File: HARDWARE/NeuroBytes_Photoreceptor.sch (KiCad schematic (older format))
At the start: 21 parts, among them P1 CONN_01X04, P2 CONN_01X04, P3 CONN_01X07, SW1 SW_PUSH, SW2 SW_PUSH, U1 APDS9007, U2 STM32L011Gx, U3 LD3985M33R

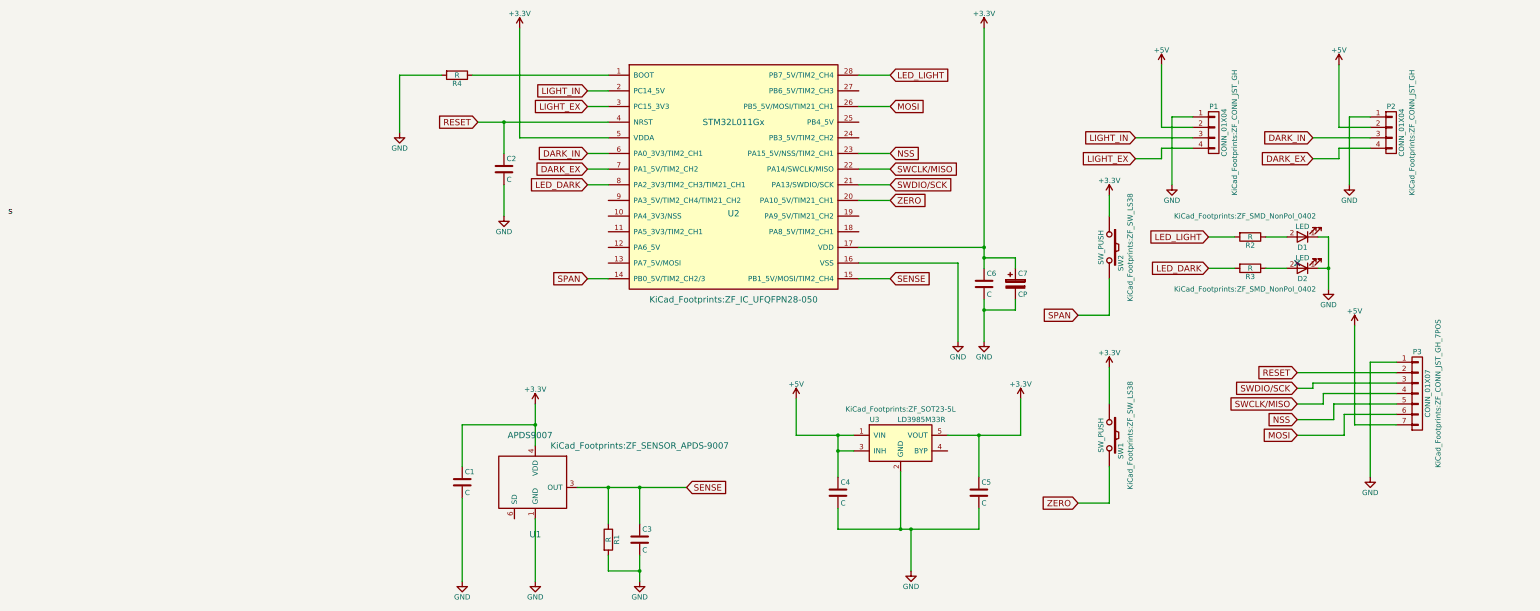
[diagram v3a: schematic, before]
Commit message: Updated Gerber files. Added BOM. Added component values to schematic. Added fiducials.
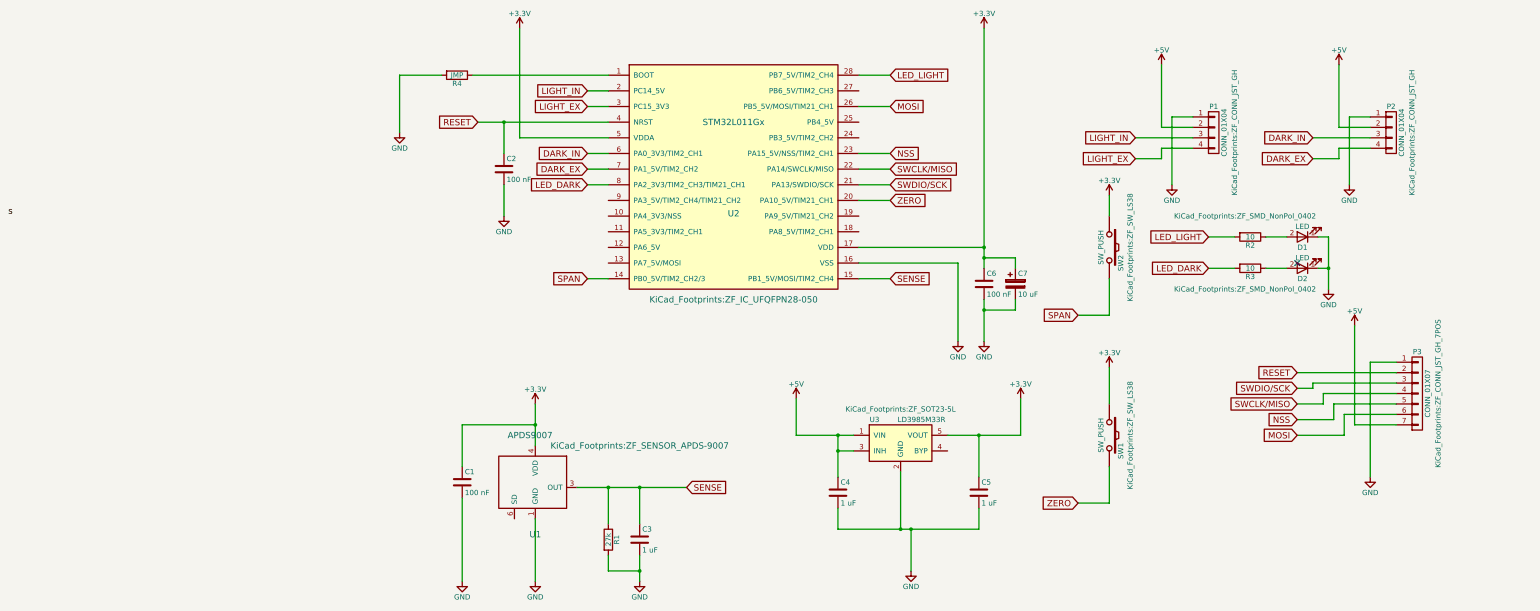
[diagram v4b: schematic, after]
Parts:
- C1, C2, C6: value C -> 100 nF; Subs Allowed No -> Yes
- C3, C4, C5: value C -> 1 uF; Subs Allowed No -> Yes
- C7: value CP -> 10 uF; Subs Allowed No -> Yes
- R1: value R -> 27k; Subs Allowed No -> Yes
- R2, R3: value R -> 10; Subs Allowed No -> Yes
- R4: value R -> JMP; Subs Allowed No -> Yes
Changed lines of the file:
@@
 Sheet 1 1
 Title "Photoreceptor"
-Date "2017-03-04"
-Rev "DRAFT"
+Date "2017-05-16"
+Rev "D"
 Comp "NeuroTinker LLC"
-Comment1 "Ordered 6 boards 3/4/2017 (3 large, 3 small)"
+Comment1 "License: GPL v3"
 Comment2 ""
 Comment3 ""
@@
 $EndComp
 $Comp
-L +5V #PWR8
+L +5V #PWR01
 U 1 1 58B9AB7F
 P 4700 4850
-F 0 "#PWR8" H 4700 4700 50  0001 C CNN
+F 0 "#PWR01" H 4700 4700 50  0001 C CNN
 F 1 "+5V" H 4700 4990 50  0000 C CNN
 F 2 "" H 4700 4850 50  0000 C CNN
@@
 P 5100 5750
 F 0 "C4" H 5125 5850 50  0000 L CNN
-F 1 "C" H 5125 5650 50  0000 L CNN
+F 1 "1 uF" H 5125 5650 50  0000 L CNN
 F 2 "KiCad_Footprints:ZF_SMD_NonPol_0603" H 5138 5600 50  0001 C CNN
 F 3 "" H 5100 5750 50  0000 C CNN
-F 4 "No" H 5100 5750 60  0001 C CNN "Subs Allowed"
+F 4 "Yes" H 5100 5750 60  0001 C CNN "Subs Allowed"
 F 5 "Yes" H 5100 5750 60  0001 C CNN "RoHS"
 	1    5100 5750
@@
 P 6450 5750
 F 0 "C5" H 6475 5850 50  0000 L CNN
-F 1 "C" H 6475 5650 50  0000 L CNN
+F 1 "1 uF" H 6475 5650 50  0000 L CNN
 F 2 "KiCad_Footprints:ZF_SMD_NonPol_0603" H 6488 5600 50  0001 C CNN
 F 3 "" H 6450 5750 50  0000 C CNN
-F 4 "No" H 6450 5750 60  0001 C CNN "Subs Allowed"
+F 4 "Yes" H 6450 5750 60  0001 C CNN "Subs Allowed"
 F 5 "Yes" H 6450 5750 60  0001 C CNN "RoHS"
 	1    6450 5750
@@
 $EndComp
 $Comp
-L +3.3V #PWR13
+L +3.3V #PWR02
 U 1 1 58B9B0DC
 P 6850 4850
-F 0 "#PWR13" H 6850 4700 50  0001 C CNN
+F 0 "#PWR02" H 6850 4700 50  0001 C CNN
 F 1 "+3.3V" H 6850 4990 50  0000 C CNN
 F 2 "" H 6850 4850 50  0000 C CNN
@@
 $EndComp
 $Comp
-L GND #PWR9
+L GND #PWR03
 U 1 1 58B9B110
 P 5800 6500
-F 0 "#PWR9" H 5800 6250 50  0001 C CNN
+F 0 "#PWR03" H 5800 6250 50  0001 C CNN
 F 1 "GND" H 5800 6350 50  0000 C CNN
 F 2 "" H 5800 6500 50  0000 C CNN
@@
 $EndComp
 $Comp
-L +3.3V #PWR4
+L +3.3V #PWR04
 U 1 1 58B9B1C8
 P 2050 1300
-F 0 "#PWR4" H 2050 1150 50  0001 C CNN
+F 0 "#PWR04" H 2050 1150 50  0001 C CNN
 F 1 "+3.3V" H 2050 1440 50  0000 C CNN
 F 2 "" H 2050 1300 50  0000 C CNN
@@
 $EndComp
 $Comp
-L +3.3V #PWR11
+L +3.3V #PWR05
 U 1 1 58B9B218
 P 6500 1300
-F 0 "#PWR11" H 6500 1150 50  0001 C CNN
+F 0 "#PWR05" H 6500 1150 50  0001 C CNN
 F 1 "+3.3V" H 6500 1440 50  0000 C CNN
 F 2 "" H 6500 1300 50  0000 C CNN
@@
 $EndComp
 $Comp
-L GND #PWR10
+L GND #PWR06
 U 1 1 58B9B234
 P 6250 4300
-F 0 "#PWR10" H 6250 4050 50  0001 C CNN
+F 0 "#PWR06" H 6250 4050 50  0001 C CNN
 F 1 "GND" H 6250 4150 50  0000 C CNN
 F 2 "" H 6250 4300 50  0000 C CNN
@@
 P 6500 3750
 F 0 "C6" H 6525 3850 50  0000 L CNN
-F 1 "C" H 6525 3650 50  0000 L CNN
+F 1 "100 nF" H 6525 3650 50  0000 L CNN
 F 2 "KiCad_Footprints:ZF_SMD_NonPol_0402_cap" H 6538 3600 50  0001 C CNN
 F 3 "" H 6500 3750 50  0000 C CNN
-F 4 "No" H 6500 3750 60  0001 C CNN "Subs Allowed"
+F 4 "Yes" H 6500 3750 60  0001 C CNN "Subs Allowed"
 F 5 "Yes" H 6500 3750 60  0001 C CNN "RoHS"
 	1    6500 3750
@@
 $EndComp
 $Comp
-L GND #PWR3
+L GND #PWR07
 U 1 1 58B9B2B4
 P 1900 3100
-F 0 "#PWR3" H 1900 2850 50  0001 C CNN
+F 0 "#PWR07" H 1900 2850 50  0001 C CNN
 F 1 "GND" H 1900 2950 50  0000 C CNN
 F 2 "" H 1900 3100 50  0000 C CNN
@@
 	5600 2800 5300 2800
 $Comp
-L +5V #PWR21
+L +5V #PWR08
 U 1 1 58B9B77D
 P 10050 4150
-F 0 "#PWR21" H 10050 4000 50  0001 C CNN
+F 0 "#PWR08" H 10050 4000 50  0001 C CNN
 F 1 "+5V" H 10050 4290 50  0000 C CNN
 F 2 "" H 10050 4150 50  0000 C CNN
@@
 $EndComp
 $Comp
-L GND #PWR22
+L GND #PWR09
 U 1 1 58B9B796
 P 10200 5600
-F 0 "#PWR22" H 10200 5350 50  0001 C CNN
+F 0 "#PWR09" H 10200 5350 50  0001 C CNN
 F 1 "GND" H 10200 5450 50  0000 C CNN
 F 2 "" H 10200 5600 50  0000 C CNN
@@
 Connection ~ 6500 3400
 $Comp
-L GND #PWR12
+L GND #PWR010
 U 1 1 58B9C6F5
 P 6500 4300
-F 0 "#PWR12" H 6500 4050 50  0001 C CNN
+F 0 "#PWR010" H 6500 4050 50  0001 C CNN
 F 1 "GND" H 6500 4150 50  0000 C CNN
 F 2 "" H 6500 4300 50  0000 C CNN
@@
 P 1900 2650
 F 0 "C2" H 1925 2750 50  0000 L CNN
-F 1 "C" H 1925 2550 50  0000 L CNN
+F 1 "100 nF" H 1925 2550 50  0000 L CNN
 F 2 "KiCad_Footprints:ZF_SMD_NonPol_0402_cap" H 1938 2500 50  0001 C CNN
 F 3 "" H 1900 2650 50  0000 C CNN
-F 4 "No" H 1900 2650 60  0001 C CNN "Subs Allowed"
+F 4 "Yes" H 1900 2650 60  0001 C CNN "Subs Allowed"
 F 5 "Yes" H 1900 2650 60  0001 C CNN "RoHS"
 	1    1900 2650
@@
 $EndComp
 $Comp
-L +5V #PWR19
+L +5V #PWR011
 U 1 1 58B9CBAC
 P 9900 1650
-F 0 "#PWR19" H 9900 1500 50  0001 C CNN
+F 0 "#PWR011" H 9900 1500 50  0001 C CNN
 F 1 "+5V" H 9900 1790 50  0000 C CNN
 F 2 "" H 9900 1650 50  0000 C CNN
@@
 	9900 2250 10200 2250
 $Comp
-L GND #PWR20
+L GND #PWR012
 U 1 1 58B9CC0C
 P 10000 2800
-F 0 "#PWR20" H 10000 2550 50  0001 C CNN
+F 0 "#PWR012" H 10000 2550 50  0001 C CNN
 F 1 "GND" H 10000 2650 50  0000 C CNN
 F 2 "" H 10000 2800 50  0000 C CNN
@@
 $EndComp
 $Comp
-L +5V #PWR16
+L +5V #PWR013
 U 1 1 58B9CEA4
 P 8200 1650
-F 0 "#PWR16" H 8200 1500 50  0001 C CNN
+F 0 "#PWR013" H 8200 1500 50  0001 C CNN
 F 1 "+5V" H 8200 1790 50  0000 C CNN
 F 2 "" H 8200 1650 50  0000 C CNN
@@
 	8200 2250 8500 2250
 $Comp
-L GND #PWR17
+L GND #PWR014
 U 1 1 58B9CEAC
 P 8300 2800
-F 0 "#PWR17" H 8300 2550 50  0001 C CNN
+F 0 "#PWR014" H 8300 2550 50  0001 C CNN
 F 1 "GND" H 8300 2650 50  0000 C CNN
 F 2 "" H 8300 2800 50  0000 C CNN
@@
 $EndComp
 $Comp
-L GND #PWR18
+L GND #PWR015
 U 1 1 58B9D2D7
 P 9800 3800
-F 0 "#PWR18" H 9800 3550 50  0001 C CNN
+F 0 "#PWR015" H 9800 3550 50  0001 C CNN
 F 1 "GND" H 9800 3650 50  0000 C CNN
 F 2 "" H 9800 3800 50  0000 C CNN
@@
 P 9050 3300
 F 0 "R2" V 9130 3300 50  0000 C CNN
-F 1 "R" V 9050 3300 50  0000 C CNN
+F 1 "10" V 9050 3300 50  0000 C CNN
 F 2 "KiCad_Footprints:ZF_SMD_NonPol_0402" V 8980 3300 50  0001 C CNN
 F 3 "" H 9050 3300 50  0000 C CNN
-F 4 "No" H 9050 3300 60  0001 C CNN "Subs Allowed"
+F 4 "Yes" H 9050 3300 60  0001 C CNN "Subs Allowed"
 F 5 "Yes" H 9050 3300 60  0001 C CNN "RoHS"
 	1    9050 3300
@@
 $EndComp
 $Comp
-L +3.3V #PWR15
+L +3.3V #PWR016
 U 1 1 58B9D7AB
 P 7700 4550
-F 0 "#PWR15" H 7700 4400 50  0001 C CNN
+F 0 "#PWR016" H 7700 4400 50  0001 C CNN
 F 1 "+3.3V" H 7700 4690 50  0000 C CNN
 F 2 "" H 7700 4550 50  0000 C CNN
@@
 $EndComp
 $Comp
-L +3.3V #PWR14
+L +3.3V #PWR017
 U 1 1 58B9D91D
 P 7700 2900
-F 0 "#PWR14" H 7700 2750 50  0001 C CNN
+F 0 "#PWR017" H 7700 2750 50  0001 C CNN
 F 1 "+3.3V" H 7700 3040 50  0000 C CNN
 F 2 "" H 7700 2900 50  0000 C CNN
@@
 $EndComp
 $Comp
-L +3.3V #PWR5
+L +3.3V #PWR018
 U 1 1 58B9DDBA
 P 2200 4900
-F 0 "#PWR5" H 2200 4750 50  0001 C CNN
+F 0 "#PWR018" H 2200 4750 50  0001 C CNN
 F 1 "+3.3V" H 2200 5040 50  0000 C CNN
 F 2 "" H 2200 4900 50  0000 C CNN
@@
 	2200 4900 2200 5300
 $Comp
-L GND #PWR6
+L GND #PWR019
 U 1 1 58B9DE4B
 P 2200 6600
-F 0 "#PWR6" H 2200 6350 50  0001 C CNN
+F 0 "#PWR019" H 2200 6350 50  0001 C CNN
 F 1 "GND" H 2200 6450 50  0000 C CNN
 F 2 "" H 2200 6600 50  0000 C CNN
@@
 P 2900 6200
 F 0 "R1" V 2980 6200 50  0000 C CNN
-F 1 "R" V 2900 6200 50  0000 C CNN
+F 1 "27k" V 2900 6200 50  0000 C CNN
 F 2 "KiCad_Footprints:ZF_SMD_NonPol_0402" V 2830 6200 50  0001 C CNN
 F 3 "" H 2900 6200 50  0000 C CNN
-F 4 "No" H 2900 6200 60  0001 C CNN "Subs Allowed"
+F 4 "Yes" H 2900 6200 60  0001 C CNN "Subs Allowed"
 F 5 "Yes" H 2900 6200 60  0001 C CNN "RoHS"
 	1    2900 6200
@@
 P 3200 6200
 F 0 "C3" H 3225 6300 50  0000 L CNN
-F 1 "C" H 3225 6100 50  0000 L CNN
+F 1 "1 uF" H 3225 6100 50  0000 L CNN
 F 2 "KiCad_Footprints:ZF_SMD_NonPol_0603" H 3238 6050 50  0001 C CNN
 F 3 "" H 3200 6200 50  0000 C CNN
-F 4 "No" H 3200 6200 60  0001 C CNN "Subs Allowed"
+F 4 "Yes" H 3200 6200 60  0001 C CNN "Subs Allowed"
 F 5 "Yes" H 3200 6200 60  0001 C CNN "RoHS"
 	1    3200 6200
@@
 $EndComp
 $Comp
-L GND #PWR7
+L GND #PWR020
 U 1 1 58B9DF7E
 P 3200 6600
-F 0 "#PWR7" H 3200 6350 50  0001 C CNN
+F 0 "#PWR020" H 3200 6350 50  0001 C CNN
 F 1 "GND" H 3200 6450 50  0000 C CNN
 F 2 "" H 3200 6600 50  0000 C CNN
@@
 P 1500 5650
 F 0 "C1" H 1525 5750 50  0000 L CNN
-F 1 "C" H 1525 5550 50  0000 L CNN
+F 1 "100 nF" H 1525 5550 50  0000 L CNN
 F 2 "KiCad_Footprints:ZF_SMD_NonPol_0402_cap" H 1538 5500 50  0001 C CNN
 F 3 "" H 1500 5650 50  0000 C CNN
-F 4 "No" H 1500 5650 60  0001 C CNN "Subs Allowed"
+F 4 "Yes" H 1500 5650 60  0001 C CNN "Subs Allowed"
 F 5 "Yes" H 1500 5650 60  0001 C CNN "RoHS"
 	1    1500 5650
@@
 Connection ~ 2200 5100
 $Comp
-L GND #PWR2
+L GND #PWR021
 U 1 1 58B9E313
 P 1500 6600
-F 0 "#PWR2" H 1500 6350 50  0001 C CNN
+F 0 "#PWR021" H 1500 6350 50  0001 C CNN
 F 1 "GND" H 1500 6450 50  0000 C CNN
 F 2 "" H 1500 6600 50  0000 C CNN
@@
 P 9050 3600
 F 0 "R3" V 9130 3600 50  0000 C CNN
-F 1 "R" V 9050 3600 50  0000 C CNN
+F 1 "10" V 9050 3600 50  0000 C CNN
 F 2 "KiCad_Footprints:ZF_SMD_NonPol_0402" V 8980 3600 50  0001 C CNN
 F 3 "" H 9050 3600 50  0000 C CNN
-F 4 "No" H 9050 3600 60  0001 C CNN "Subs Allowed"
+F 4 "Yes" H 9050 3600 60  0001 C CNN "Subs Allowed"
 F 5 "Yes" H 9050 3600 60  0001 C CNN "RoHS"
 	1    9050 3600
@@
 P 1450 1750
 F 0 "R4" V 1530 1750 50  0000 C CNN
-F 1 "R" V 1450 1750 50  0000 C CNN
+F 1 "JMP" V 1450 1750 50  0000 C CNN
 F 2 "KiCad_Footprints:ZF_SMD_NonPol_0402" V 1380 1750 50  0001 C CNN
 F 3 "" H 1450 1750 50  0000 C CNN
-F 4 "No" H 1450 1750 60  0001 C CNN "Subs Allowed"
+F 4 "Yes" H 1450 1750 60  0001 C CNN "Subs Allowed"
 F 5 "Yes" H 1450 1750 60  0001 C CNN "RoHS"
 	1    1450 1750
@@
 $EndComp
 $Comp
-L GND #PWR1
+L GND #PWR022
 U 1 1 590B4A9C
 P 900 2300
-F 0 "#PWR1" H 900 2050 50  0001 C CNN
+F 0 "#PWR022" H 900 2050 50  0001 C CNN
 F 1 "GND" H 900 2150 50  0000 C CNN
 F 2 "" H 900 2300 50  0000 C CNN
@@
 P 6800 3750
 F 0 "C7" H 6825 3850 50  0000 L CNN
-F 1 "CP" H 6825 3650 50  0000 L CNN
+F 1 "10 uF" H 6825 3650 50  0000 L CNN
 F 2 "KiCad_Footprints:ZF_SMD_pol_1206" H 6838 3600 50  0001 C CNN
 F 3 "" H 6800 3750 50  0000 C CNN
-F 4 "No" H 6800 3750 60  0001 C CNN "Subs Allowed"
+F 4 "Yes" H 6800 3750 60  0001 C CNN "Subs Allowed"
 F 5 "Yes" H 6800 3750 60  0001 C CNN "RoHS"
 	1    6800 3750

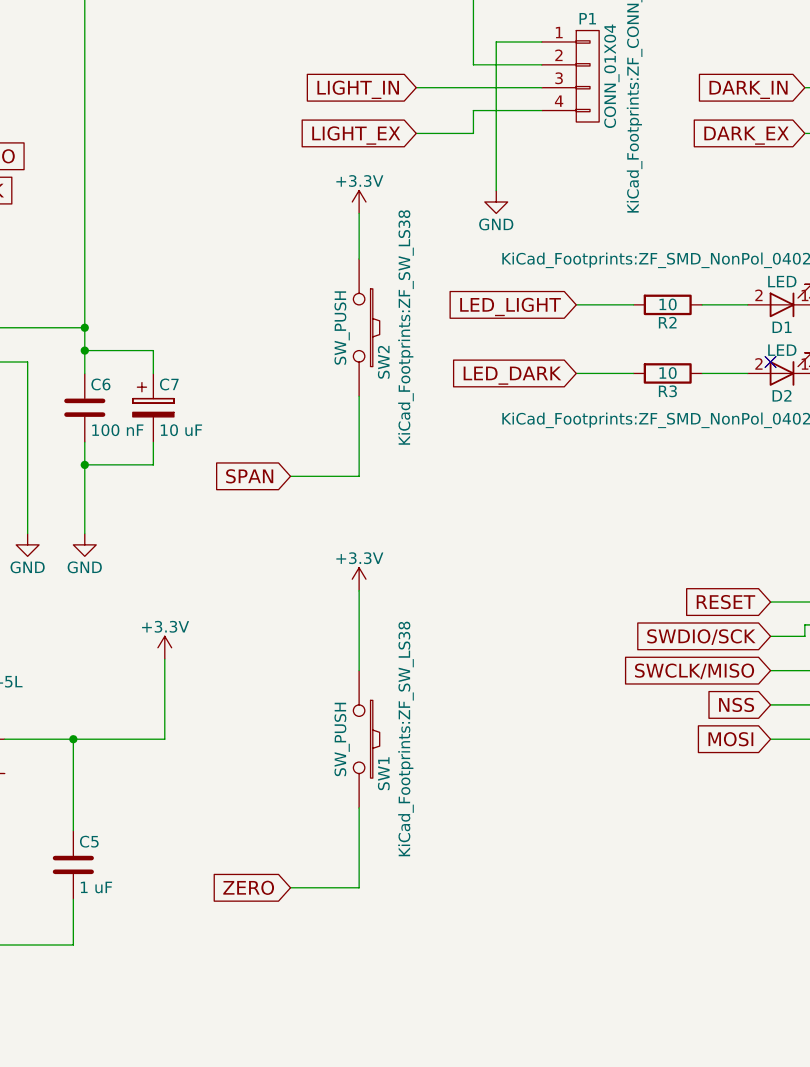
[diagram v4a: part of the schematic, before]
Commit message: Updated swith footprint.
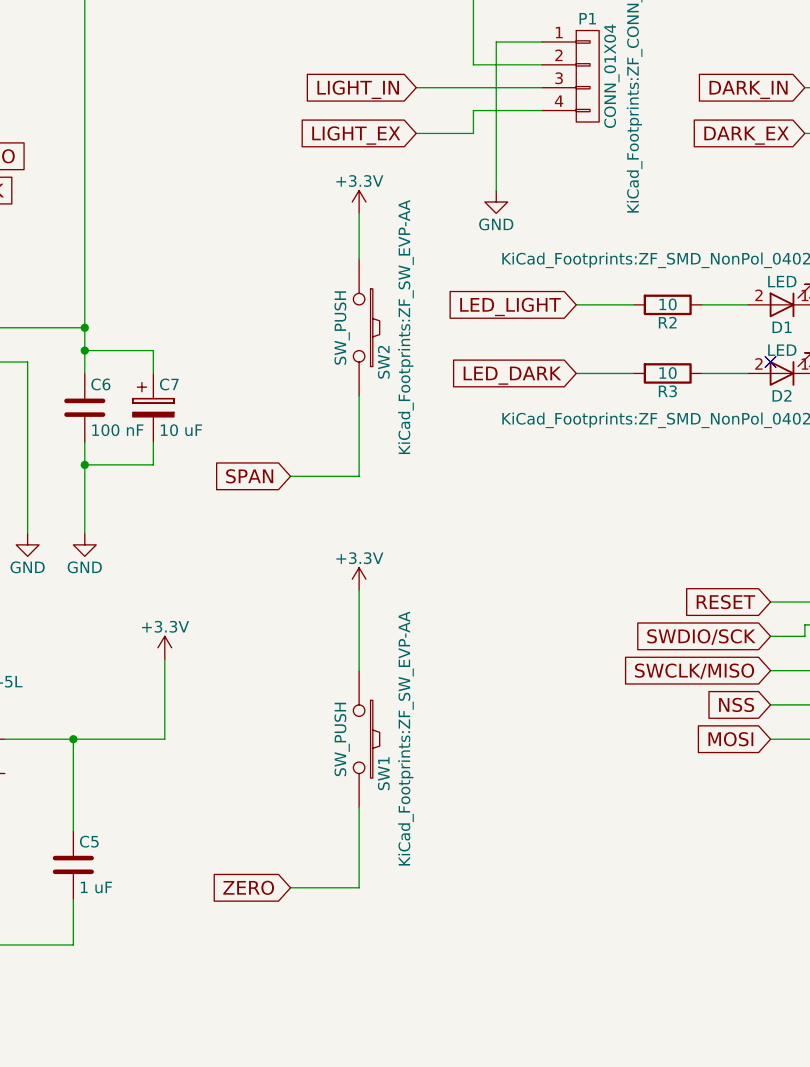
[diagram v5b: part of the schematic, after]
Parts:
- SW1, SW2: footprint KiCad_Footprints:ZF_SW_LS38 -> KiCad_Footprints:ZF_SW_EVP-AA
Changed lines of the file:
@@
 F 0 "SW2" H 7850 3510 50  0000 C CNN
 F 1 "SW_PUSH" H 7700 3320 50  0000 C CNN
-F 2 "KiCad_Footprints:ZF_SW_LS38" H 7700 3600 50  0000 C CNN
+F 2 "KiCad_Footprints:ZF_SW_EVP-AA" H 7700 3600 50  0000 C CNN
 F 3 "" H 7700 3400 50  0000 C CNN
 F 4 "No" H 7700 3400 60  0001 C CNN "Subs Allowed"
@@
 F 0 "SW1" H 7850 5310 50  0000 C CNN
 F 1 "SW_PUSH" H 7700 5120 50  0000 C CNN
-F 2 "KiCad_Footprints:ZF_SW_LS38" H 7700 5400 50  0000 C CNN
+F 2 "KiCad_Footprints:ZF_SW_EVP-AA" H 7700 5400 50  0000 C CNN
 F 3 "" H 7700 5200 50  0000 C CNN
 F 4 "No" H 7700 5200 60  0001 C CNN "Subs Allowed"
